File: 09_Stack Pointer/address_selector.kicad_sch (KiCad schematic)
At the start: 1 part, among them U6 74LS245

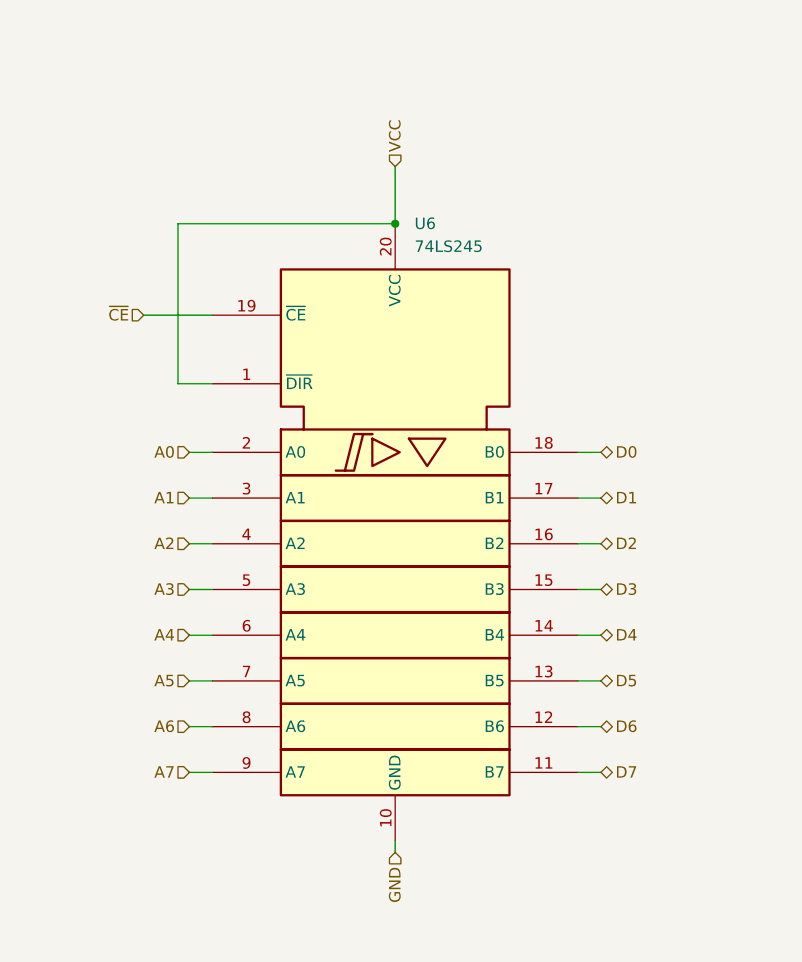
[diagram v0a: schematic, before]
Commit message: Last revision of the cpu, all boards have been ordered. Implementation to be tested and documented in following commits.
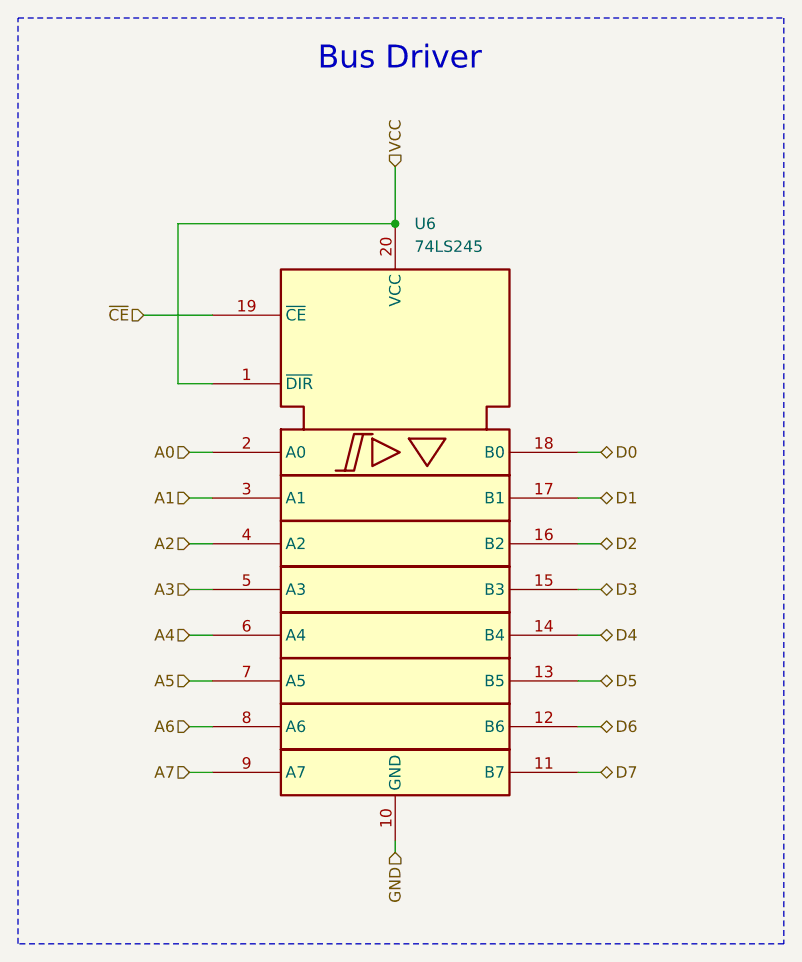
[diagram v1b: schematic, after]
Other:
- note added: "Bus Driver"
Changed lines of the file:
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@@
 		(rev "1.0")
 		(company "Marco Vettigli")
+		(comment 2 "By using or distributing it, you accept the terms of the GPL.")
+		(comment 3 "It comes with absolutely NO WARRANTY; for details, see the full license.")
+		(comment 4 "This software is licensed under the GNU General Public License (GPL).")
+	)
+	(rectangle
+		(start 113.03 43.18)
+		(end 198.12 146.05)
+		(stroke
+			(width 0)
+			(type dash)
+		)
+		(fill
+			(type none)
+		)
+	)
+	(text "Bus Driver"
+		(exclude_from_sim no)
+		(at 155.448 47.752 0)
+		(effects
+			(font
+				(size 2.54 2.54)
+			)
+		)
 	)
 	(junction
